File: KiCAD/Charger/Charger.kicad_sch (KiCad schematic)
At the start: 9 parts, among them J1 Conn_01x09_Socket, J2 Conn_01x04_Socket, J3 Conn_01x04_Socket, J4 Conn_01x05_Socket, J5 Conn_01x05_Pin, J6 Conn_01x04_Pin, J7 Conn_01x04_Pin, U1 ESP32-S3-DevKitC, U2 CR2013-MI2120

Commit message: Update shematics
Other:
- added sheet Fan-Control (fan-control.kicad_sch)
- company: (none) -> Andreas Wansner
- title: (none) -> 3 Phase Charge controller
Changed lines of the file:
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@@
 	(generator_version "10.0")
 	(paper "A4")
+	(title_block
+		(title "3 Phase Charge controller")
+		(company "Andreas Wansner")
+	)
 	(symbol
 		(lib_id "Connector:Conn_01x09_Socket")
@@
 				)
 			)
+		)
+	)
+	(sheet
+		(at 15.24 171.45)
+		(size 41.91 22.86)
+		(exclude_from_sim no)
+		(in_bom yes)
+		(on_board yes)
+		(dnp no)
+		(fields_autoplaced yes)
+		(stroke
+			(width 0.1524)
+			(type solid)
+		)
+		(fill
+			(color 0 0 0 0)
+		)
+		(property "Sheetname" "Fan-Control"
+			(at 15.24 170.7384 0)
+			(show_name no)
+			(do_not_autoplace no)
+			(effects
+				(font
+					(size 1.27 1.27)
+				)
+				(justify left bottom)
+			)
+		)
+		(property "Sheetfile" "fan-control.kicad_sch"
+			(at 15.24 194.8946 0)
+			(show_name no)
+			(do_not_autoplace no)
+			(effects
+				(font
+					(size 1.27 1.27)
+				)
+				(justify left top)
+			)
+		)
+		(instances
+			(project "Charger"
+				(path "/7a93e01a-90df-4a46-8b10-5e4e0c5ef05c"
+					(page "2")
+				)
+			)

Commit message: Update shematic
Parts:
- removed J4: Conn_01x05_Socket, symbol Connector:Conn_01x05_Socket
- removed J6, J7: Conn_01x04_Pin, symbol Connector:Conn_01x04_Pin
- added C1: 470u, Capacitor_THT:CP_Radial_D8.0mm_P3.50mm, symbol Device:C_Polarized_Small
- added C2: 100n, Capacitor_THT:C_Disc_D5.0mm_W2.5mm_P5.00mm, symbol Device:C_Small
- added F1: 500mA, Fuse:Fuseholder_Clip-5x20mm_Bel_FC-203-22_Lateral_P17.80x5.00mm_D1.17mm_Horizontal, symbol Device:Fuse_Small
- added J1: Screw_Terminal_01x02, TerminalBlock_WAGO:TerminalBlock_WAGO_236-402_1x02_P5.00mm_45Degree, symbol Connector:Screw_Terminal_01x02
- J100: renamed from J1; footprint (none) -> Connector_JST:JST_XH_B9B-XH-AM_1x09_P2.50mm_Vertical
- J2, J3: footprint (none) -> Connector_JST:JST_XH_B4B-XH-AM_1x04_P2.50mm_Vertical
- J5: footprint (none) -> Connector_JST:JST_XH_B5B-XH-AM_1x05_P2.50mm_Vertical
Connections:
- new net: F1.1, J1.1 (Pin_1)
- new net +12V: C1.1, C2.1, F1.2
- new net GND: C1.2, C2.2, J1.2 (Pin_2)
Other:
- moved on the sheet: J100, J2, J3, J5, U1

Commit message: Update shematics
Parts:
- added R13: 120, Resistor_THT:R_Axial_DIN0207_L6.3mm_D2.5mm_P7.62mm_Horizontal, symbol Device:R_Small
- added R14: 10k, Resistor_THT:R_Axial_DIN0207_L6.3mm_D2.5mm_P7.62mm_Horizontal, symbol Device:R_Small
- added U3: SN65HVD230, Package_SO:SOIC-8_3.9x4.9mm_P1.27mm, symbol Interface_CAN_LIN:SN65HVD230
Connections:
- net GND: now also R14.2, U3.2 (GND)
- new net: R13.2, U3.6 (CANL)
- new net: R13.1, U3.7 (CANH)
- new net: R14.1, U3.8 (Rs)
- new net +3.3V: U3.3 (VCC)
- new net CAN_RX: U3.4 (R)
- new net CAN_TX: U3.1 (D)

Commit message: Update shematics
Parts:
- J2: value Conn_01x04_Socket -> I²C 1
- J3: value Conn_01x04_Socket -> I²C 2
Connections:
- net +3.3V: now also J2.2 (Pin_2), J3.2 (Pin_2), U1.1 (3V3), U1.2 (3V3), U2.1 (VCC)
- net CAN_RX: now also U1.9 (GPIO16/ADC2_CH5/32K_N)
- net CAN_TX: now also U1.8 (GPIO15/ADC2_CH4/32K_P)
- net GND: now also J2.1 (Pin_1), J3.1 (Pin_1), U1.22 (GND), U1.23 (GND), U1.24 (GND), U1.44 (GND), U2.2 (GND)
- net SCl: now reaches J3.3 (Pin_3)
- net SCl: now also J2.3 (Pin_3), U1.15 (GPIO9/ADC1_CH8)
- net SDA: now reaches J3.4 (Pin_4)
- net SDA: now also J2.4 (Pin_4), U1.12 (GPIO8/ADC1_CH7)
- net TFT_CS: now reaches U2.3 (~{CS})
- net TFT_CS: now also U1.5 (GPIO5/ADC1_CH4)
- net TFT_RESET: now reaches U2.4 (RESET)
- net TFT_RESET: now also U1.6 (GPIO6/ADC1_CH5)
- net TFT_DC: now reaches U2.5 (D/~{C})
- net TFT_DC: now also U1.7 (GPIO7/ADC1_CH6)
- net SPI_MOSI: now reaches U2.6 (MOSI)
- net SPI_MOSI: now also U1.17 (GPIO11/ADC2_CH0)
- net SPI_CLK: now reaches U2.7 (SCK)
- net SPI_CLK: now also U1.19 (GPIO13/ADC2_CH2)
- net TFT_BL_PWM: now reaches U2.8 (LED)
- net TFT_BL_PWM: now also U1.4 (GPIO4/ADC1_CH3)
- net SPI_MISO: now reaches U2.9 (MISO)
- net SPI_MISO: now also U1.18 (GPIO12/ADC2_CH1)
- net ENC_A: now reaches U1.10 (GPIO17/ADC2_CH6)
- net ENC_B: now reaches U1.11 (GPIO18/ADC2_CH7)
- net RES_2: now reaches U1.16 (GPIO10/ADC1_CH9)
- net RES_3: now reaches U1.20 (GPIO14/ADC2_CH3)
- net +5V: now reaches U1.21 (5V)
- net FAN_ENABLE: now reaches U1.27 (GPIO21)
- net FAN3_TACH: now reaches U1.36 (GPIO39/MTCK)
- net FAN2_TACH: now reaches U1.37 (GPIO40/MTDO)
- net FAN1_TACH: now reaches U1.38 (GPIO41/MTDI)
- net FAN_PWM: now reaches U1.39 (GPIO42/MTMS)
- net ENC_BTN: now reaches U1.40 (GPIO2/ADC1_CH1)
- net RES_1: now reaches U1.41 (GPIO1/ADC1_CH0)
- no-connect marks 0 -> 24
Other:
- moved on the sheet: R13, R14, U1, U2, U3

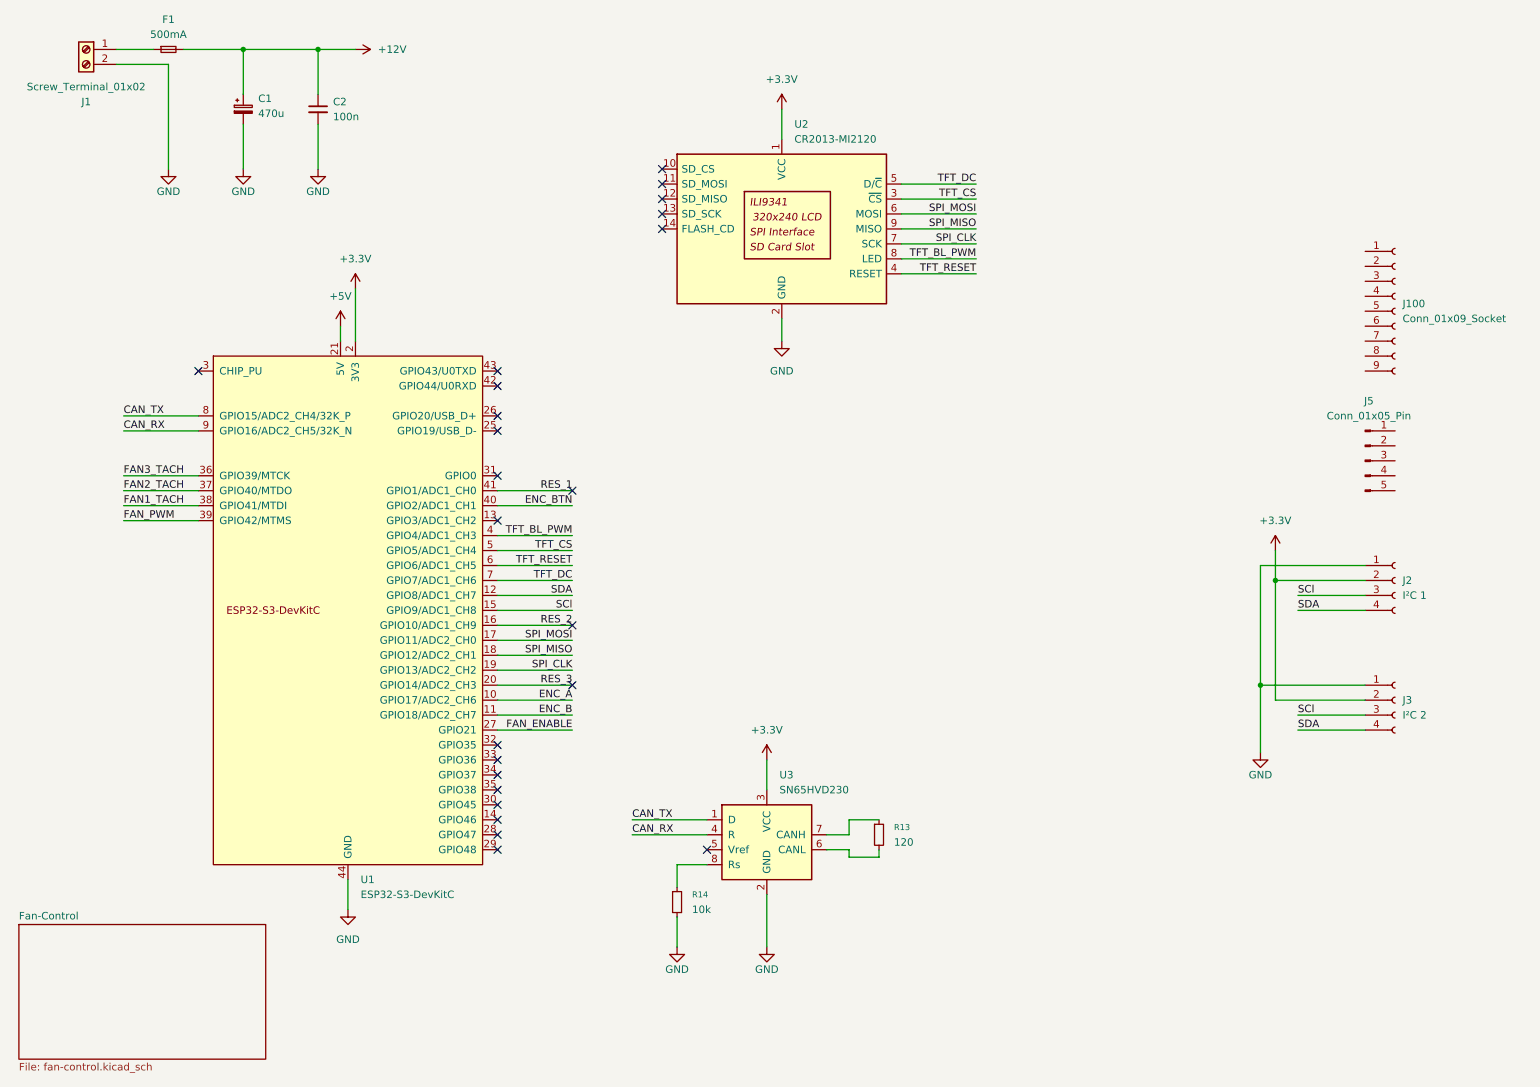
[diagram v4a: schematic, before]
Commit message: Work on KiCAD project
- most of the electronics are now in ready made modules
- removed second page, everything fits in one page now
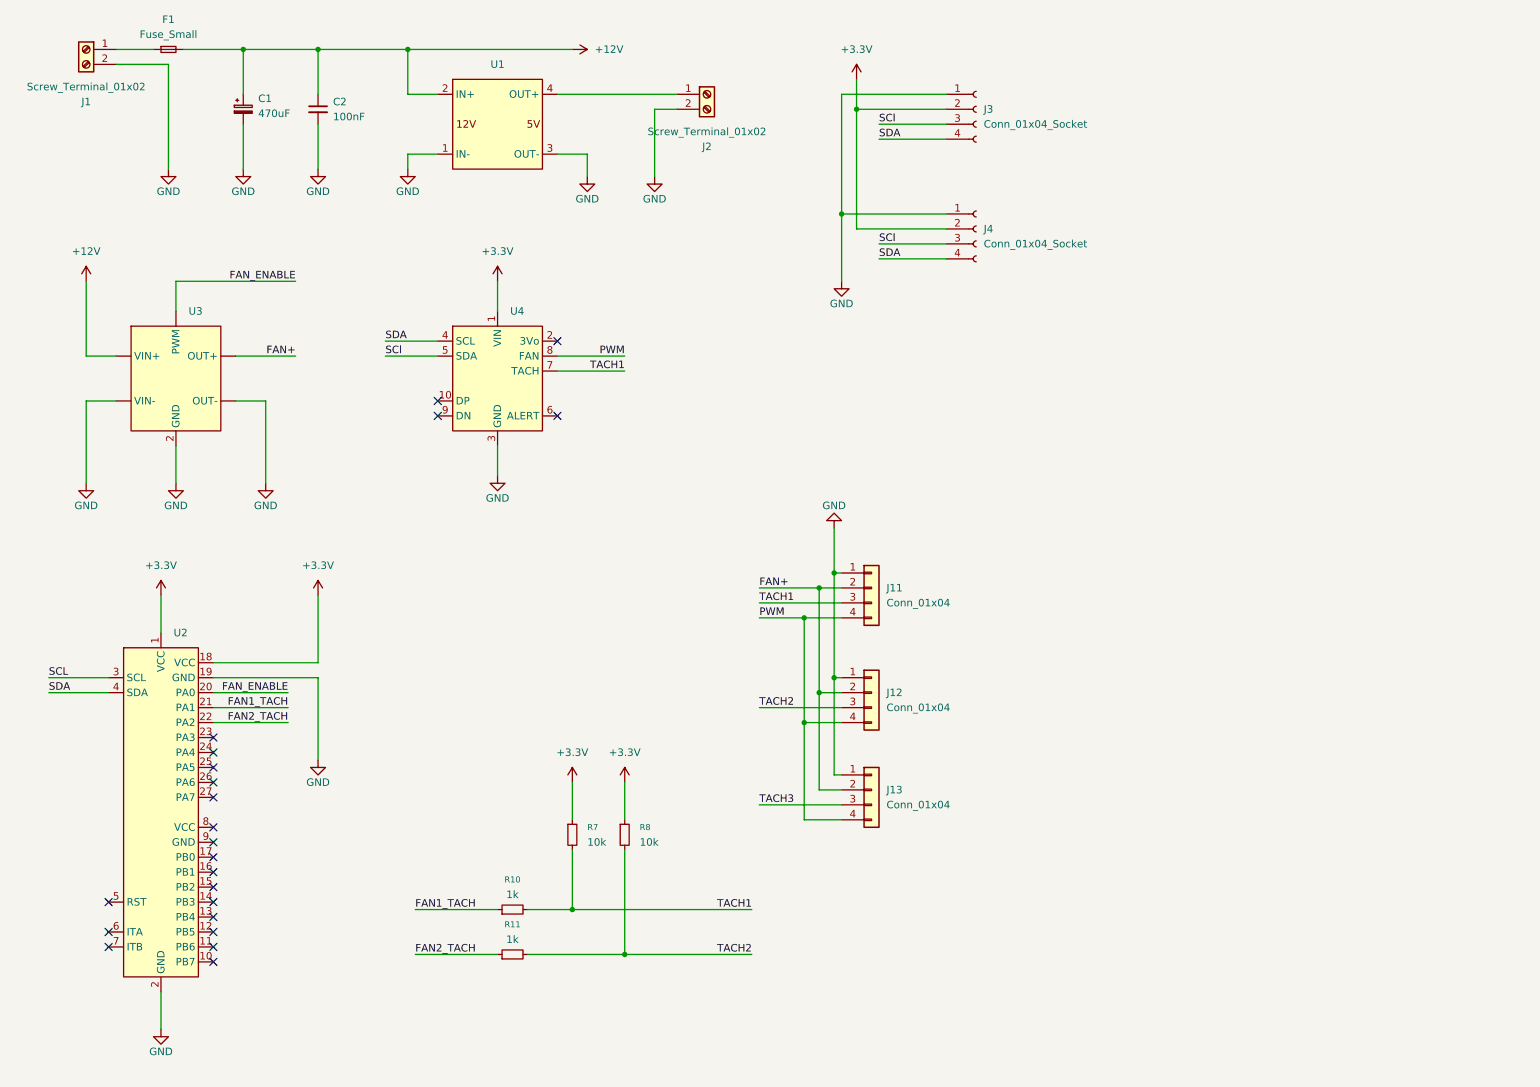
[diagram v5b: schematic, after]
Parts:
- removed J100: Conn_01x09_Socket, Connector_JST:JST_XH_B9B-XH-AM_1x09_P2.50mm_Vertical, symbol Connector:Conn_01x09_Socket
- removed J5: Conn_01x05_Pin, Connector_JST:JST_XH_B5B-XH-AM_1x05_P2.50mm_Vertical, symbol Connector:Conn_01x05_Pin
- removed R13: 120, Resistor_THT:R_Axial_DIN0207_L6.3mm_D2.5mm_P7.62mm_Horizontal, symbol Device:R_Small
- removed R14: 10k, Resistor_THT:R_Axial_DIN0207_L6.3mm_D2.5mm_P7.62mm_Horizontal, symbol Device:R_Small
- removed U1: ESP32-S3-DevKitC, PCM_Espressif:ESP32-S3-DevKitC, symbol PCM_Espressif:ESP32-S3-DevKitC
- removed U2: CR2013-MI2120, Display:CR2013-MI2120, symbol Driver_Display:CR2013-MI2120
- removed U3: SN65HVD230, Package_SO:SOIC-8_3.9x4.9mm_P1.27mm, symbol Interface_CAN_LIN:SN65HVD230
- added J11, J12, J13: Conn_01x04, Connector:FanPinHeader_1x04_P2.54mm_Vertical, symbol Connector_Generic:Conn_01x04
- added J2: Screw_Terminal_01x02, TerminalBlock_WAGO:TerminalBlock_WAGO_236-402_1x02_P5.00mm_45Degree, symbol Connector:Screw_Terminal_01x02
- added R10, R11: 1k, Resistor_THT:R_Axial_DIN0207_L6.3mm_D2.5mm_P7.62mm_Horizontal, symbol Device:R_Small
- added R7, R8: 10k, Resistor_THT:R_Axial_DIN0207_L6.3mm_D2.5mm_P7.62mm_Horizontal, symbol Device:R_Small
- added U1: (no value), Charger:DC-DC, symbol Charger:DC-DC
- added U2: (no value), Charger:MCP23017, symbol Charger:MCP23017
- added U3: (no value), Charger:MOSFET, symbol Charger:MOSFET
- added U4: (no value), Charger:EMC2101, symbol Charger:EMC2101
- C1: value 470u -> 470uF
- C2: value 100n -> 100nF
- F1: value 500mA -> Fuse_Small
- J3: renamed from J2; value I²C 1 -> Conn_01x04_Socket
- J4: renamed from J3; value I²C 2 -> Conn_01x04_Socket
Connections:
- net +12V: now also U1.2 (IN+), U3. (OUT-)
- net +3.3V: now also R7.1, R8.1, U2.1 (VCC), U2.18 (VCC), U4.1 (VIN)
- net FAN1_TACH: now also R10.1, U2.21 (PA1)
- net FAN2_TACH: now also R11.1, U2.22 (PA2)
- net FAN_ENABLE: now also U2.20 (PA0), U3. (OUT-)
- net GND: now also J11.1 (Pin_1), J12.1 (Pin_1), J13.1 (Pin_1), J2.2 (Pin_2), U1.1 (IN-), U1.3 (OUT-), U2.19 (GND), U2.2 (GND), U3. (OUT-), U3.2 (GND), U4.3 (GND)
- net SCl: now also U4.5 (SDA)
- net SDA: now also U2.4 (SDA), U4.4 (SCL)
- new net: J2.1 (Pin_1), U1.4 (OUT+)
- new net FAN+: J11.2 (Pin_2), J12.2 (Pin_2), J13.2 (Pin_2), U3. (OUT-)
- new net PWM: J11.4 (Pin_4), J12.4 (Pin_4), J13.4 (Pin_4), U4.8 (FAN)
- new net SCL: U2.3 (SCL)
- new net TACH1: J11.3 (Pin_3), R10.2, R7.2, U4.7 (TACH)
- new net TACH2: J12.3 (Pin_3), R11.2, R8.2
- new net TACH3: J13.3 (Pin_3)
- no-connect marks 24 -> 22
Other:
- removed sheet Fan-Control
- moved on the sheet: J3, J4
